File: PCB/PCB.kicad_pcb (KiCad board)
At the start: 2 copper layers, 82 parts, among them J1 GND, J10 VM1, J11 GND, J12 VM2, J13 GND, J14 P3B, J15 GND, J16 P3A, J17 NEXTION, J18 Power, J19 OneWire, J2 pump, J20 I2C, J21 USB_B, J3 GND, J4 LED, J5 GND, J6 P12B, J7 GND, J8 P12A, J9 GND, Q1 S8050, Q10 IRLR2905, Q2 S8050, Q3 IRLR2905, Q4 IRLR2905, Q5 IRLR2905, Q6 IRLR2905, Q7 IRLR2905, Q8 IRLR2905, Q9 IRLR2905, U1 ESP32-WROOM-32, X1 12MHz

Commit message: pcb update #4
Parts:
- moved 5Vstabilizer1 218.1 mm to (-47.0, 65.8)
- moved J5 217.6 mm to (-69.6, 68.6)
- moved C3 217.5 mm to (-103.4, 111.0)
- moved C5 217.5 mm to (-14.3, 68.0)
- moved C6 217.5 mm to (-78.1, 109.8)
- moved C9 217.5 mm to (-93.3, 107.8)
- moved CH340G1 217.5 mm to (-36.1, 69.4)
- moved D1 217.5 mm to (-102.2, 107.1)
- moved F1 217.5 mm to (-20.9, 66.7)
- moved H1 217.5 mm to (-60.6, 108.6)
- moved H2 217.5 mm to (-41.3, 84.8)
- moved H3 217.5 mm to (-14.0, 59.4)
- moved H4 217.5 mm to (-28.2, 67.9)
- moved J10 217.5 mm to (-96.4, 83.2)
- moved J11 217.5 mm to (-69.4, 56.8)
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
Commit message: pcb dimensions and mounting holes #4
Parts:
- 3V3stabilizer1, 5Vstabilizer1, C1, C2, C3, C4, C5, C6, C7, C8, CH340G1, D1, D2, F1, Power1, Q1, Q2, R1, R10, R11, R12, R13, R14, R15, R16, R17, R18, R19, R2, R20, R21, R3, R4, R5, R6, R7, R8, R9, RXD1, TXD1, U1, X1, signal1: moved to B.Cu
- moved J16 312.4 mm to (193.0, 127.1), turned to 90 degrees
- moved fan_1 284.1 mm to (203.2, 73.7), turned to 180 degrees
- moved fan_3 283.3 mm to (203.2, 94.0), turned to 180 degrees
- moved J13 279.5 mm to (177.8, 127.1), turned to 90 degrees
- moved J14 277.4 mm to (182.9, 127.0), turned to 90 degrees
- moved Q10 274.3 mm to (191.8, 108.2)
- moved J9 271.4 mm to (152.4, 127.1), turned to 90 degrees
- moved C9 268.9 mm to (175.3, 94.0)
- moved J15 268.4 mm to (188.0, 127.1), turned to 90 degrees
- moved U1 265.1 mm to (146.6, 6.62), turned to 90 degrees
- moved H1 264.8 mm to (203.2, 132.1)
- moved J19 262.5 mm to (175.3, 62.2), turned to 90 degrees
- moved J12 261.3 mm to (167.6, 127.1), turned to 90 degrees
- moved J8 260.8 mm to (142.2, 127.0), turned to 90 degrees
- moved J10 257.6 mm to (157.5, 127.1), turned to 90 degrees
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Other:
- board outline added: 121.4 x 90.9 mm

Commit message: pcb update #4
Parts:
- moved J17 64.3 mm to (200.7, 95.2), turned to 180 degrees
- moved C9 61.4 mm to (235.2, 80.5)
- moved fan_1 54.7 mm to (152.4, 53.3)
- moved fan_2 48.8 mm to (165.1, 53.3)
- moved fan_3 47.9 mm to (177.8, 53.3)
- moved J20 46.0 mm to (201.9, 81.3), turned to 180 degrees
- moved J19 26.9 mm to (201.9, 66.0), turned to 180 degrees
- moved Power1 10.5 mm to (63.5, 20.3)
- moved J18 10.2 mm to (189.2, 52.1)
- moved signal1 3.59 mm to (71.1, 35.6)
- renumbered MODE1 to MODE, RESET1 to RESET

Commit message: pcb update #4
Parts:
- L7805: renamed from 5Vstabilizer1; value L7805 -> 5Vstabilizer
- LF33: renamed from 3V3stabilizer1; value LF33_TO252 -> 3V3stabilizer
- moved R18 180.2 mm to (187.5, 102.9), turned to 180 degrees
- moved R19 170.3 mm to (175.3, 102.9), turned to 180 degrees
- moved R16 167.4 mm to (136.7, 102.9), turned to 180 degrees
- moved R20 149.0 mm to (162.1, 102.9), turned to 180 degrees
- moved R21 140.9 mm to (148.4, 102.9), turned to 180 degrees
- moved R15 139.9 mm to (99.3, 102.9), turned to 180 degrees
- moved R14 129.5 mm to (111.5, 102.9), turned to 180 degrees
- moved X1 121.0 mm to (61.6, 83.8)
- moved R17 116.8 mm to (123.0, 102.9), turned to 180 degrees
- moved R12 103.8 mm to (54.4, 52.1)
- moved R1 94.8 mm to (186.5, 27.9)
- moved R9 94.1 mm to (120.7, 35.6)
- moved C3 92.1 mm to (33.1, 31.9)
- moved D1 92.1 mm to (34.3, 35.7)
- moved C2 92.1 mm to (50.9, 33.1)
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- renumbered CH340G1 to CH340G, U1 to ESP32-WROOM32, Power1 to Power, RXD1 to RXD, signal1 to Signal, TXD1 to TXD
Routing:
- net GND: track 0.00 -> 361.6 mm, vias 0 -> 40
- net Net-(J6-Pad1): track 0.00 -> 56.0 mm, vias 0 -> 5
- net Net-(J4-Pad1): track 0.00 -> 55.8 mm, vias 0 -> 5
- net Net-(J8-Pad1): track 0.00 -> 55.8 mm, vias 0 -> 5
- net Net-(J10-Pad1): track 0.00 -> 52.2 mm, vias 0 -> 5
- net Net-(J2-Pad1): track 0.00 -> 52.0 mm, vias 0 -> 5
- net Net-(J14-Pad1): track 0.00 -> 52.0 mm, vias 0 -> 5
- net Net-(J16-Pad1): track 0.00 -> 51.5 mm, vias 0 -> 5
- net Net-(J12-Pad1): track 0.00 -> 51.5 mm, vias 0 -> 5

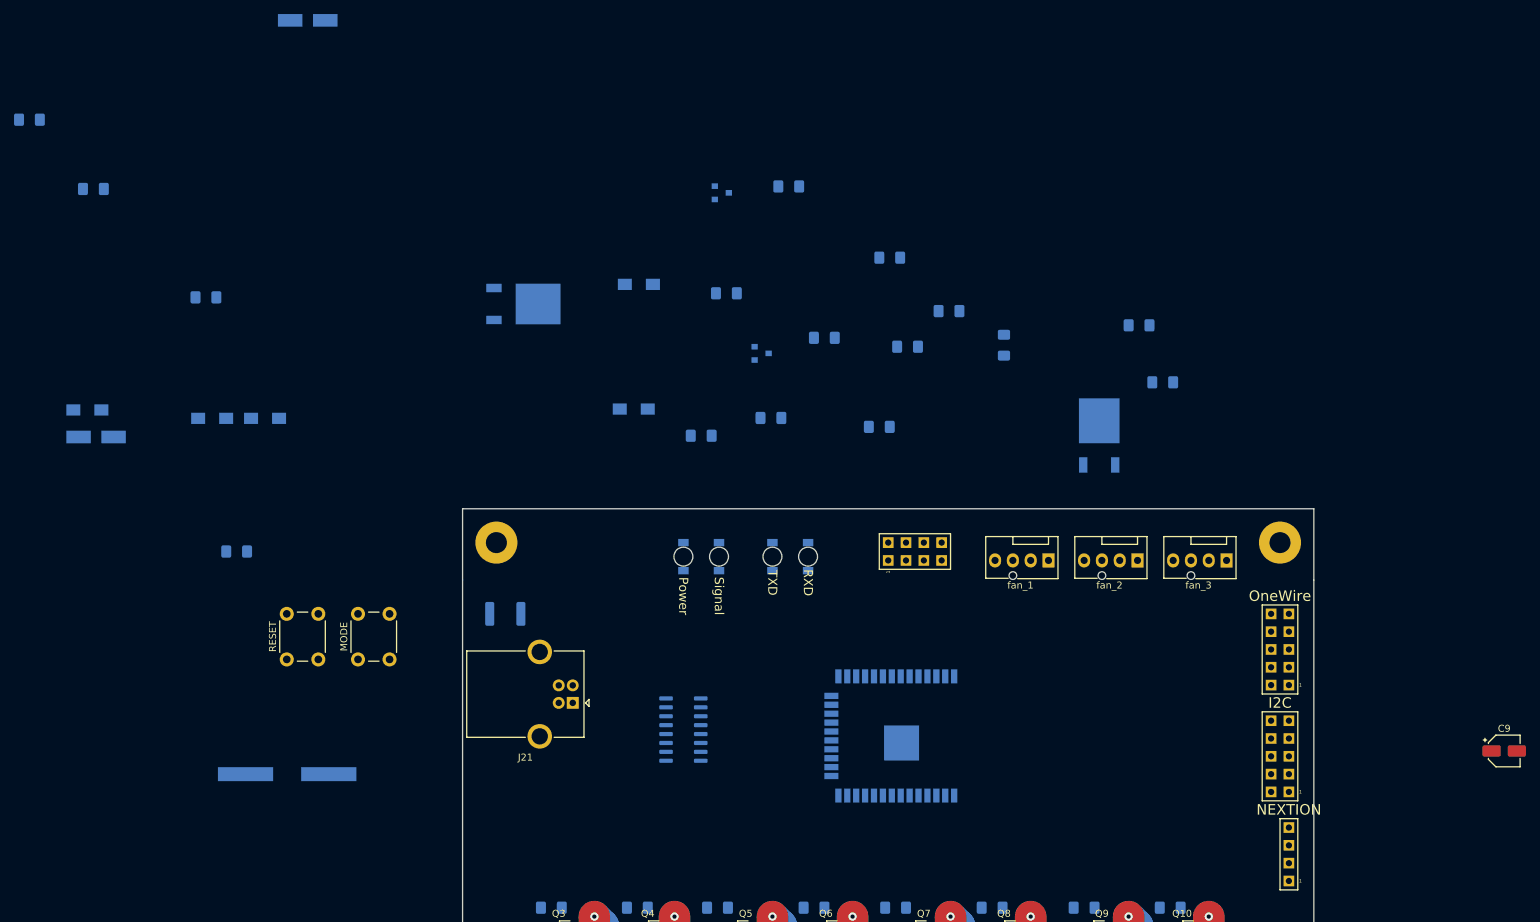
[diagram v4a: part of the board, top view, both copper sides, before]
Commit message: components added into board #4
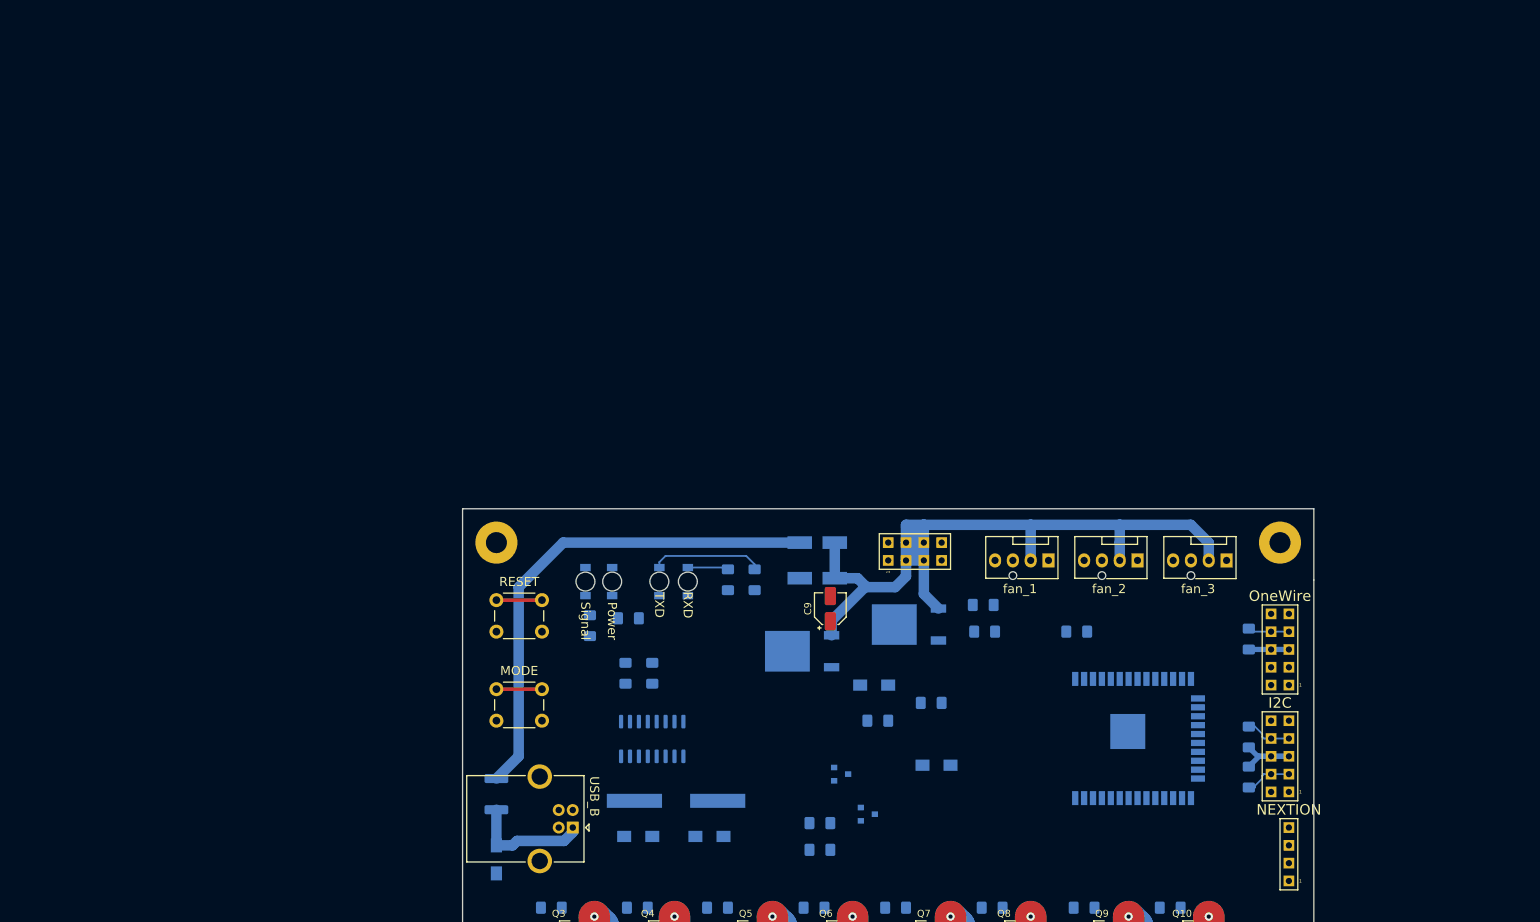
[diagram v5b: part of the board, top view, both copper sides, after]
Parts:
- moved C4 153.8 mm to (174.2, 63.5), turned to 180 degrees
- moved R11 150.9 mm to (137.6, 90.8), turned to 180 degrees
- moved C7 118.5 mm to (153.5, 73.7)
- moved D1 104.8 mm to (137.2, 55.9), turned to 180 degrees
- moved D2 104.1 mm to (137.2, 50.8), turned to 180 degrees
- moved C9 98.2 mm to (139.1, 60.2), turned to 90 degrees
- moved C6 94.8 mm to (145.3, 71.1)
- moved R10 94.7 mm to (137.6, 94.6)
- moved C3 86.7 mm to (91.4, 96.0), turned to 270 degrees
- moved C2 85.1 mm to (111.7, 92.7)
- moved Q1 84.6 mm to (140.6, 83.8)
- moved C8 80.7 mm to (154.2, 82.5)
- moved R2 79.0 mm to (198.8, 84.2), turned to 270 degrees
- moved R6 69.0 mm to (124.5, 56.1), turned to 270 degrees
- moved Q2 67.4 mm to (144.4, 89.5)
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- renumbered J21 to USB_B
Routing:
- net +12V: track 0.00 -> 118.3 mm
- net +5V: track 0.00 -> 71.3 mm
- net +3V3: track 0.00 -> 18.3 mm
- net Net-(C3-Pad1): track 0.00 -> 17.4 mm
- net Net-(R7-Pad1): track 0.00 -> 15.9 mm
- net /I2C_SDA: track 0.00 -> 6.87 mm
- net /I2C_SCL: track 0.00 -> 6.67 mm
- net /IO_0: track 0.00 -> 6.50 mm
- net /EN: track 0.00 -> 6.50 mm
- net /OneWire: track 0.00 -> 5.90 mm
- net Net-(R6-Pad1): track 0.00 -> 5.82 mm

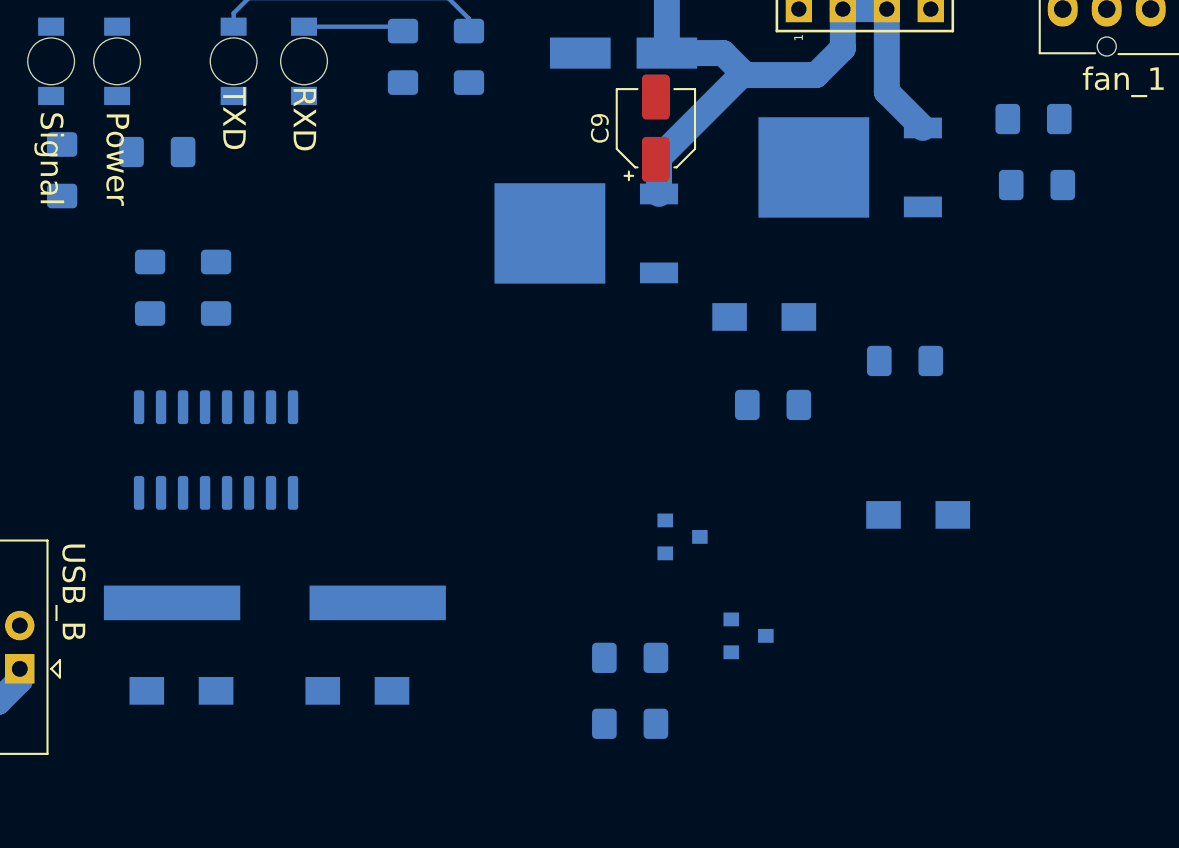
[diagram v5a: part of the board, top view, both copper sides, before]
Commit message: reset circuit #4
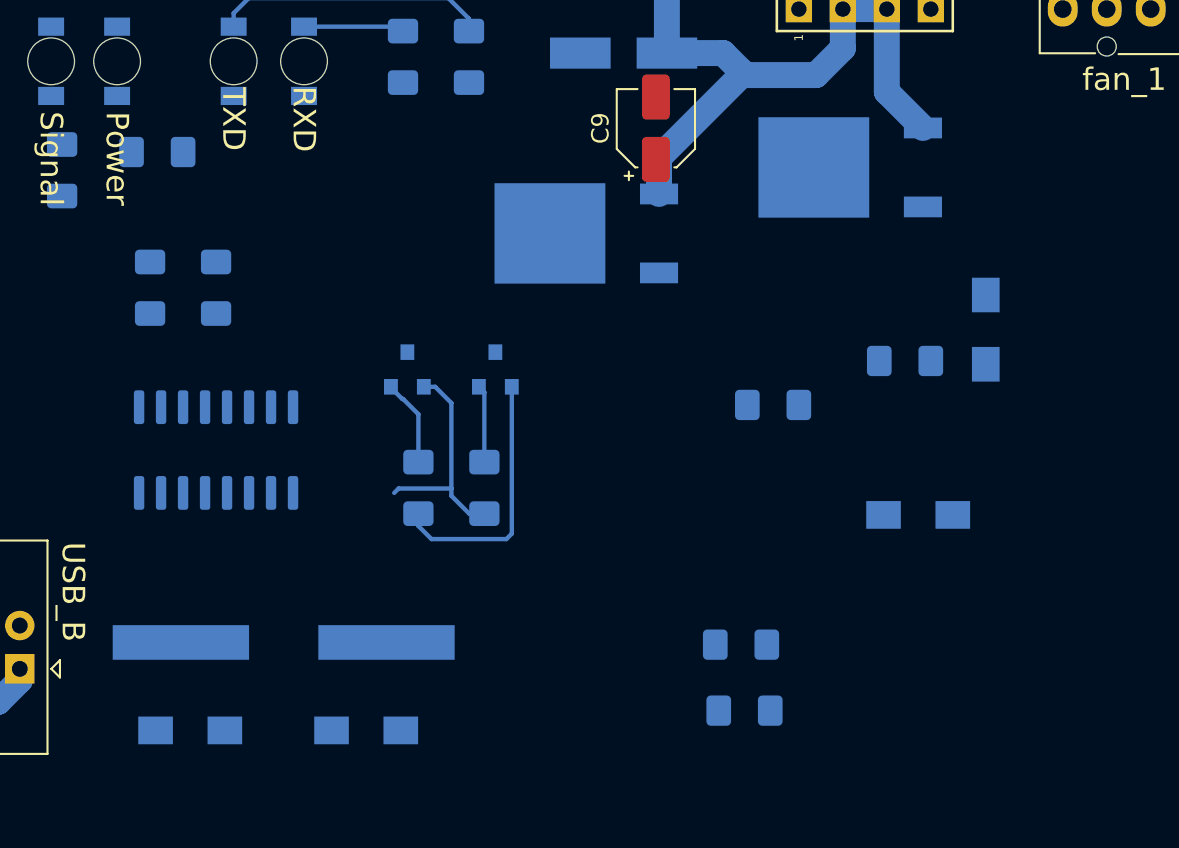
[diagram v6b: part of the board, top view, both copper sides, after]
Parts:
- moved R4 34.7 mm to (144.0, 90.0)
- moved R5 34.7 mm to (144.2, 93.9)
- moved Q2 21.2 mm to (129.8, 74.2), turned to 90 degrees
- moved Q1 18.6 mm to (124.7, 74.2), turned to 90 degrees
- moved R10 18.3 mm to (125.3, 81.0), turned to 270 degrees
- moved R11 12.9 mm to (129.2, 81.0), turned to 270 degrees
- moved C6 12.8 mm to (158.1, 71.8), turned to 270 degrees
- moved C1 2.34 mm to (122.3, 95.0)
- moved C2 2.34 mm to (112.2, 95.0)
- moved X1 2.34 mm to (117.6, 89.9)
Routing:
- net Net-(CH340G1-Pad13): track 0.00 -> 15.0 mm
- net Net-(CH340G1-Pad14): track 0.00 -> 13.1 mm
- net Net-(Q1-Pad2): track 0.00 -> 5.04 mm
- net Net-(Q2-Pad2): track 0.00 -> 4.48 mm

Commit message: indication LED #4
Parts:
- moved C5 32.5 mm to (175.2, 62.2), turned to 180 degrees
- moved C8 16.3 mm to (158.5, 66.8), turned to 270 degrees
- moved C6 13.7 mm to (158.5, 58.1), turned to 90 degrees
- moved Q1 12.8 mm to (134.4, 82.5)
- moved R11 12.8 mm to (138.8, 89.4)
- moved R10 12.8 mm to (135.0, 89.4)
- moved Q2 12.8 mm to (139.4, 82.5)
- moved R7 12.6 mm to (119.1, 64.8)
- moved C7 10.0 mm to (144.8, 68.6)
- moved R12 9.24 mm to (105.7, 64.8)
- moved R6 8.84 mm to (122.9, 64.8)
- moved R13 8.24 mm to (104.4, 75.6), turned to 180 degrees
- moved R9 5.17 mm to (109.5, 64.8)
- moved TXD 4.64 mm to (119.3, 57.1), turned to 90 degrees
- moved RXD 4.64 mm to (123.3, 57.1), turned to 90 degrees
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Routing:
- net /TXD: track 0.00 -> 89.7 mm
- net /RXD: track 0.00 -> 84.8 mm
- net +3V3: track 18.3 -> 89.7 mm
- net /s_LED: track 0.00 -> 61.9 mm
- net /IO_0: track 6.50 -> 62.3 mm, vias 0 -> 1
- net /EN: track 6.50 -> 60.4 mm
- net Net-(CH340G1-Pad2): track 0.00 -> 41.4 mm
- net Net-(CH340G1-Pad3): track 0.00 -> 39.0 mm
- net Net-(CH340G1-Pad13): track 15.0 -> 44.3 mm
- net Net-(CH340G1-Pad14): track 13.1 -> 38.7 mm
- net Net-(C1-Pad1): track 0.00 -> 22.6 mm
- net /USB_P: track 0.00 -> 19.6 mm
- net /USB_N: track 0.00 -> 17.1 mm
- net Net-(C2-Pad1): track 0.00 -> 15.3 mm
- net /OneWire: track 5.90 -> 19.6 mm
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
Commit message: pcb finish #4
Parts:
- added G***: LOGO, EM:logo_5mm, B.Cu at (91.4, 108.0)
- added G***: LOGO, EM:logo_5mm, F.Cu at (101.6, 50.8)
- added G***: LOGO, EM:logo_20mm, F.Cu at (168.9, 73.7)
- added REF**: WEEE-Logo_5.6x8mm_SilkScreen, Symbol:WEEE-Logo_5.6x8mm_SilkScreen, B.Cu at (157.5, 79.4)
- added REF**: ESD-Logo_8.9x8mm_SilkScreen, Symbol:ESD-Logo_8.9x8mm_SilkScreen, F.Cu at (123.2, 91.4)
- added REF**: RoHS-Logo_6mm_SilkScreen, Symbol:RoHS-Logo_6mm_SilkScreen, B.Cu at (203.2, 114.3)
- moved R15 37.1 mm to (135.9, 96.7), turned to 90 degrees
- moved R18 33.2 mm to (154.9, 96.7), turned to 90 degrees
- moved R19 24.9 mm to (151.1, 96.7), turned to 90 degrees
- moved R14 21.4 mm to (132.1, 96.7), turned to 90 degrees
- moved R17 17.8 mm to (139.7, 96.7), turned to 90 degrees
- moved R20 16.0 mm to (147.3, 96.7), turned to 90 degrees
- moved R21 12.1 mm to (158.8, 96.7), turned to 90 degrees
- moved R16 9.13 mm to (143.5, 96.7), turned to 90 degrees
- moved C9 8.50 mm to (147.3, 62.2), turned to 270 degrees
- moved Q1 4.68 mm to (135.4, 78.0)
- moved Q2 4.68 mm to (140.5, 78.0)
- moved R10 4.68 mm to (136.0, 84.8)
- moved R11 4.68 mm to (139.8, 84.8)
- moved R4 4.68 mm to (148.1, 84.9)
- moved R5 4.68 mm to (144.3, 84.9)
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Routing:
- net +3V3: track 89.7 -> 243.4 mm, vias 0 -> 5
- net /VM2: track 0.00 -> 90.8 mm
- net /display_Vin: track 0.00 -> 87.9 mm, vias 0 -> 2
- net /LED: track 0.00 -> 70.8 mm
- net /pump: track 0.00 -> 68.0 mm
- net /IO_0: track 62.3 -> 114.3 mm, vias 1 -> 2
- net /EN: track 60.4 -> 105.1 mm, vias 0 -> 2
- net Net-(Q3-Pad1): track 0.00 -> 43.0 mm, vias 0 -> 1
- net /s_LED: track 61.9 -> 104.7 mm
- net /P12A: track 0.00 -> 42.8 mm
- net /P12B: track 0.00 -> 42.6 mm
- net Net-(Q10-Pad1): track 0.00 -> 37.9 mm, vias 0 -> 1
- net /P3B: track 0.00 -> 37.5 mm
- net /VM1: track 0.00 -> 36.3 mm
- net /OneWire: track 19.6 -> 55.2 mm
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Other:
- board text added: "3V3"
- board text added: "5V"
- board text added: "DATA"
- board text added: "E32CB_R2"
- board text added: "GND"
- board text added: "Power +12V"
- board text added: "RXD"
- board text added: "SCL"
- board text added: "SDA"
- board text added: "TXD"
- board text added: "Vilém Raška 2020"
